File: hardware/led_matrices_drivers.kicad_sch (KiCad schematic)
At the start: 12 parts, among them U6 MAX7219, U7 MAX7219, U8 MAX7219, U9 MAX7219

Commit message: Electric Rules Check completed.
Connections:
- net Mat1A.SEG_A renamed ${MAT1A}.SEG_A

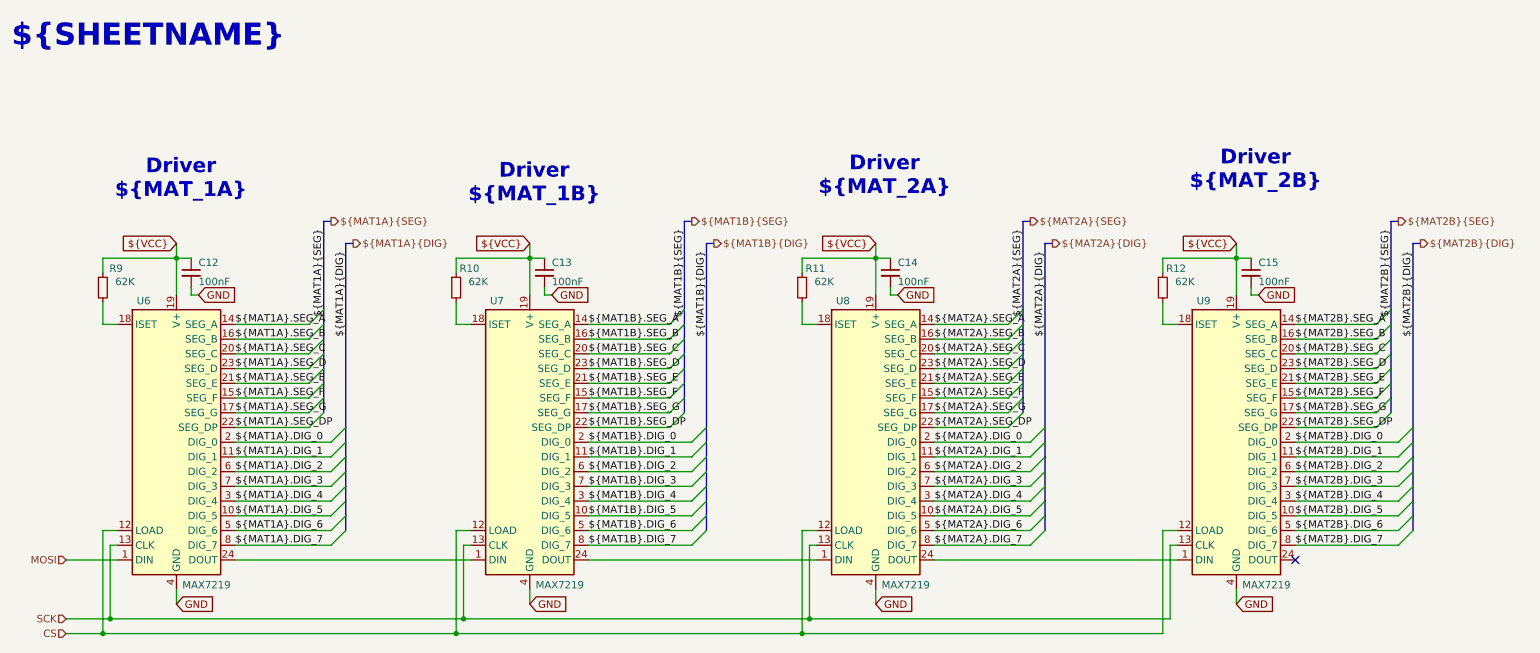
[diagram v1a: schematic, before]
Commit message: Added footprints to mounting holes and selected a part for the test LED.
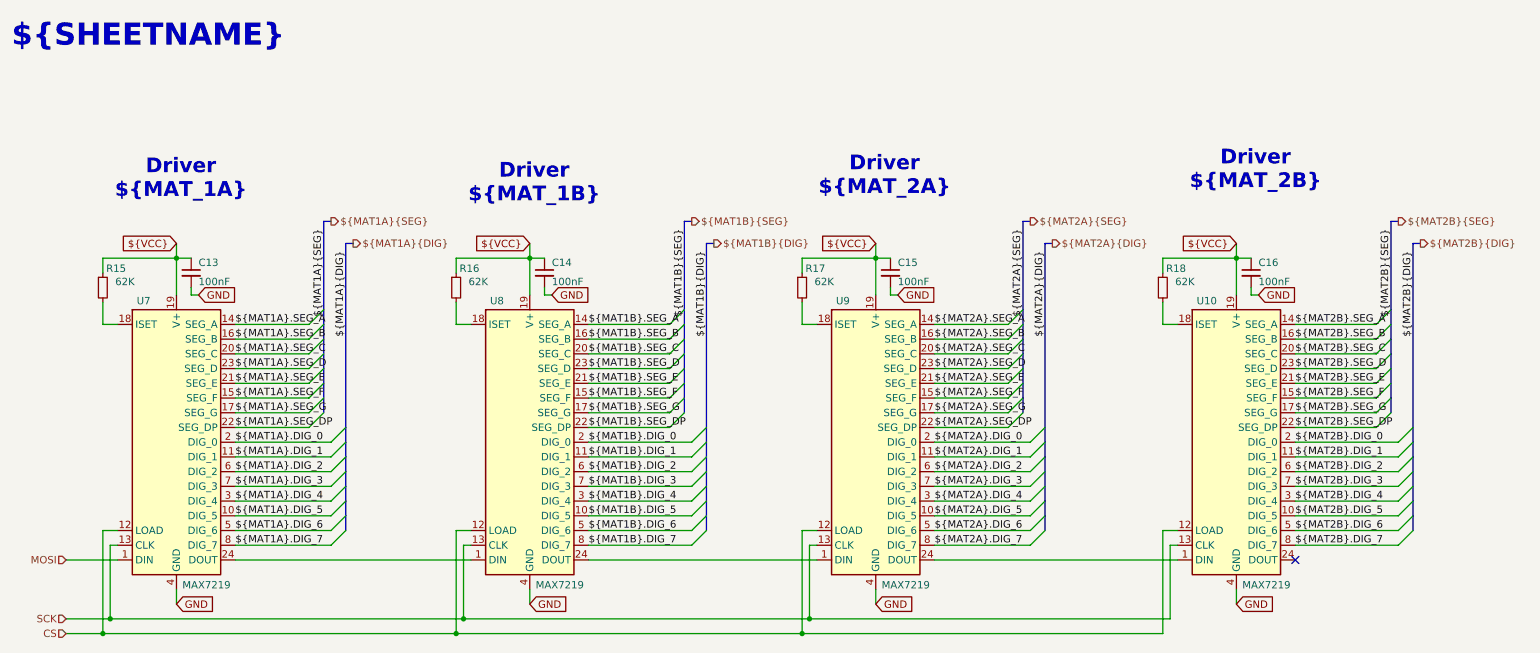
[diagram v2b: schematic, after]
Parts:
- renumbered C12 to C13, C13 to C14, C14 to C15, C15 to C16, R9 to R15, R10 to R16, R11 to R17, R12 to R18, U9 to U10, U6 to U7, U7 to U8, U8 to U9

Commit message: Added a pull up resistor to the CS line on the SPI and added two more test LEDs
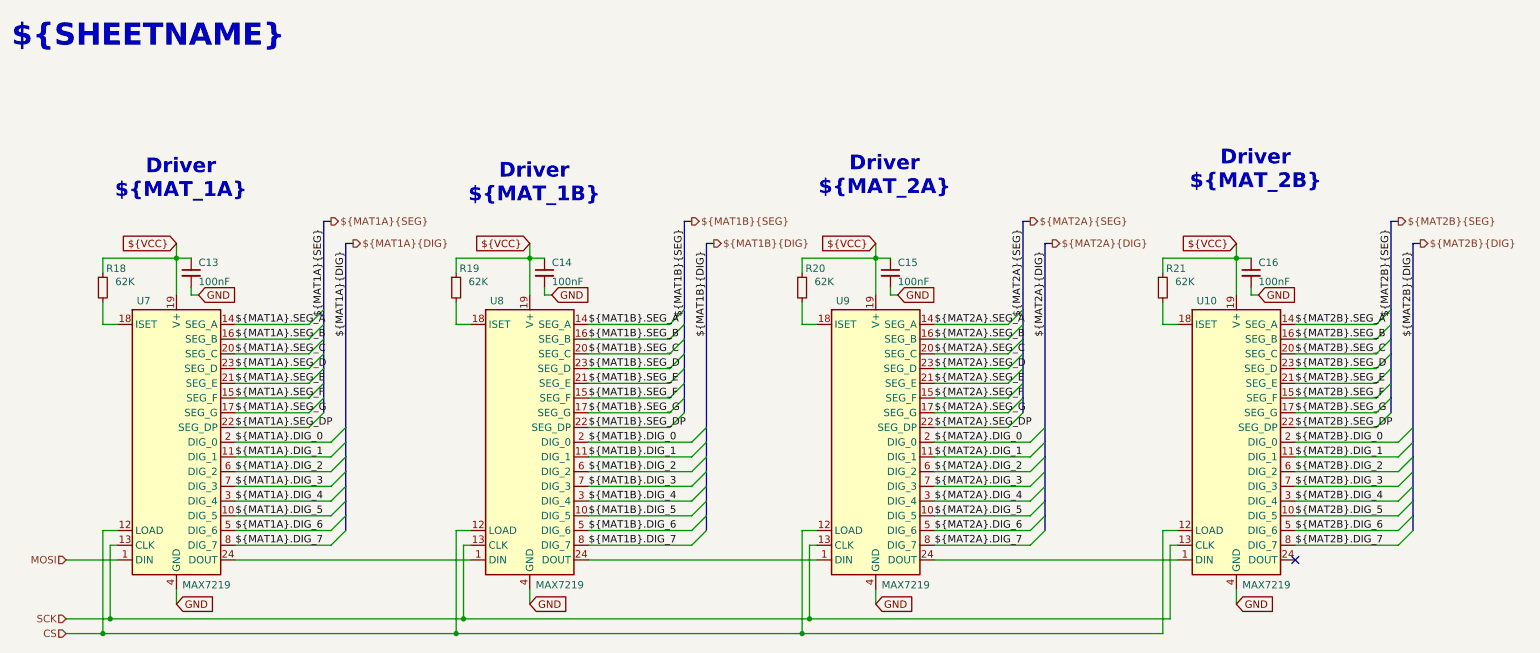
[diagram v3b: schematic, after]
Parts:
- renumbered R15 to R18, R16 to R19, R17 to R20, R18 to R21
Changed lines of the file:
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@@
 					(size 1.27 1.27)
 				)
+				(hide yes)
 			)
 		)
@@
 					(size 1.27 1.27)
 				)
+				(hide yes)
 			)
 		)
@@
 					(size 1.27 1.27)
 				)
+				(hide yes)
 			)
 		)
@@
 					(size 1.27 1.27)
 				)
+				(hide yes)
 			)
 		)
@@
 		(on_board yes)
 		(dnp no)
-		(property "Reference" "R17"
+		(property "Reference" "R20"
 			(at 157.226 64.008 0)
 			(effects
@@
 					(size 1.27 1.27)
 				)
+				(hide yes)
 			)
 		)
@@
 					(size 1.27 1.27)
 				)
+				(hide yes)
 			)
 		)
@@
 					(size 1.27 1.27)
 				)
+				(hide yes)
 			)
 		)
@@
 					(size 1.27 1.27)
 				)
+				(hide yes)
 			)
 		)
@@
 			(project "kitchen_timer-hardware"
 				(path "/8963deea-96bc-4401-b671-98fbe9ed9c6a/452e0bb3-d328-4d26-8f2f-0fdd90f8dd22"
-					(reference "R17")
+					(reference "R20")
 					(unit 1)
 				)
@@
 		(on_board yes)
 		(dnp no)
-		(property "Reference" "R16"
+		(property "Reference" "R19"
 			(at 97.536 64.008 0)
 			(effects
@@
 					(size 1.27 1.27)
 				)
+				(hide yes)
 			)
 		)
@@
 					(size 1.27 1.27)
 				)
+				(hide yes)
 			)
 		)
@@
 					(size 1.27 1.27)
 				)
+				(hide yes)
 			)
 		)
@@
 					(size 1.27 1.27)
 				)
+				(hide yes)
 			)
 		)
@@
 			(project "kitchen_timer-hardware"
 				(path "/8963deea-96bc-4401-b671-98fbe9ed9c6a/452e0bb3-d328-4d26-8f2f-0fdd90f8dd22"
-					(reference "R16")
+					(reference "R19")
 					(unit 1)
 				)
@@
 					(size 1.27 1.27)
 				)
+				(hide yes)
 			)
 		)
@@
 					(size 1.27 1.27)
 				)
+				(hide yes)
 			)
 		)
@@
 					(size 1.27 1.27)
 				)
+				(hide yes)
 			)
 		)
@@
 					(size 1.27 1.27)
 				)
+				(hide yes)
 			)
 		)
@@
 		(on_board yes)
 		(dnp no)
-		(property "Reference" "R15"
+		(property "Reference" "R18"
 			(at 36.576 64.008 0)
 			(effects
@@
 					(size 1.27 1.27)
 				)
+				(hide yes)
 			)
 		)
@@
 					(size 1.27 1.27)
 				)
+				(hide yes)
 			)
 		)
@@
 					(size 1.27 1.27)
 				)
+				(hide yes)
 			)
 		)
@@
 					(size 1.27 1.27)
 				)
+				(hide yes)
 			)
 		)
@@
 			(project ""
 				(path "/8963deea-96bc-4401-b671-98fbe9ed9c6a/452e0bb3-d328-4d26-8f2f-0fdd90f8dd22"
-					(reference "R15")
+					(reference "R18")
 					(unit 1)
 				)
@@
 					(size 1.27 1.27)
 				)
+				(hide yes)
 			)
 		)
@@
 					(size 1.27 1.27)
 				)
+				(hide yes)
 			)
 		)
@@
 					(size 1.27 1.27)
 				)
+				(hide yes)
 			)
 		)
@@
 					(size 1.27 1.27)
 				)
+				(hide yes)
 			)
 		)
@@
 					(size 1.27 1.27)
 				)
+				(hide yes)
 			)
 		)
@@
 					(size 1.27 1.27)
 				)
+				(hide yes)
 			)
 		)
@@
 					(size 1.27 1.27)
 				)
+				(hide yes)
 			)
 		)
@@
 					(size 1.27 1.27)
 				)
+				(hide yes)
 			)
 		)
@@
 					(size 1.27 1.27)
 				)
+				(hide yes)
 			)
 		)
@@
 					(size 1.27 1.27)
 				)
+				(hide yes)
 			)
 		)
@@
 					(size 1.27 1.27)
 				)
+				(hide yes)
 			)
 		)
@@
 					(size 1.27 1.27)
 				)
+				(hide yes)
 			)
 		)
@@
 					(size 1.27 1.27)
 				)
+				(hide yes)
 			)
 		)
@@
 					(size 1.27 1.27)
 				)
+				(hide yes)
 			)
 		)
@@
 					(size 1.27 1.27)
 				)
+				(hide yes)
 			)
 		)
@@
 					(size 1.27 1.27)
 				)
+				(hide yes)
 			)
 		)
@@
 					(size 1.27 1.27)
 				)
+				(hide yes)
 			)
 		)
@@
 					(size 1.27 1.27)
 				)
+				(hide yes)
 			)
 		)
@@
 					(size 1.27 1.27)
 				)
+				(hide yes)
 			)
 		)
@@
 					(size 1.27 1.27)
 				)
+				(hide yes)
 			)
 		)
@@
 					(size 1.27 1.27)
 				)
+				(hide yes)
 			)
 		)
@@
 					(size 1.27 1.27)
 				)
+				(hide yes)
 			)
 		)
@@
 					(size 1.27 1.27)
 				)
+				(hide yes)
 			)
 		)
@@
 					(size 1.27 1.27)
 				)
+				(hide yes)
 			)
 		)
@@
 		(on_board yes)
 		(dnp no)
-		(property "Reference" "R18"
+		(property "Reference" "R21"
 			(at 219.456 64.008 0)
 			(effects
@@
 					(size 1.27 1.27)
 				)
+				(hide yes)
 			)
 		)
@@
 					(size 1.27 1.27)
 				)
+				(hide yes)
 			)
 		)
@@
 					(size 1.27 1.27)
 				)
+				(hide yes)
 			)
 		)
@@
 					(size 1.27 1.27)
 				)
+				(hide yes)
 			)
 		)
@@
 			(project "kitchen_timer-hardware"
 				(path "/8963deea-96bc-4401-b671-98fbe9ed9c6a/452e0bb3-d328-4d26-8f2f-0fdd90f8dd22"
-					(reference "R18")
+					(reference "R21")
 					(unit 1)
 				)
